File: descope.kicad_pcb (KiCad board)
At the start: 2 copper layers, 26.9 x 31.8 mm, 19 parts, among them Q1 2N3906, Q2 2N3904, Q3 2N3906, Q4 2N3904, Q5 2N3906, Q6 2N3904

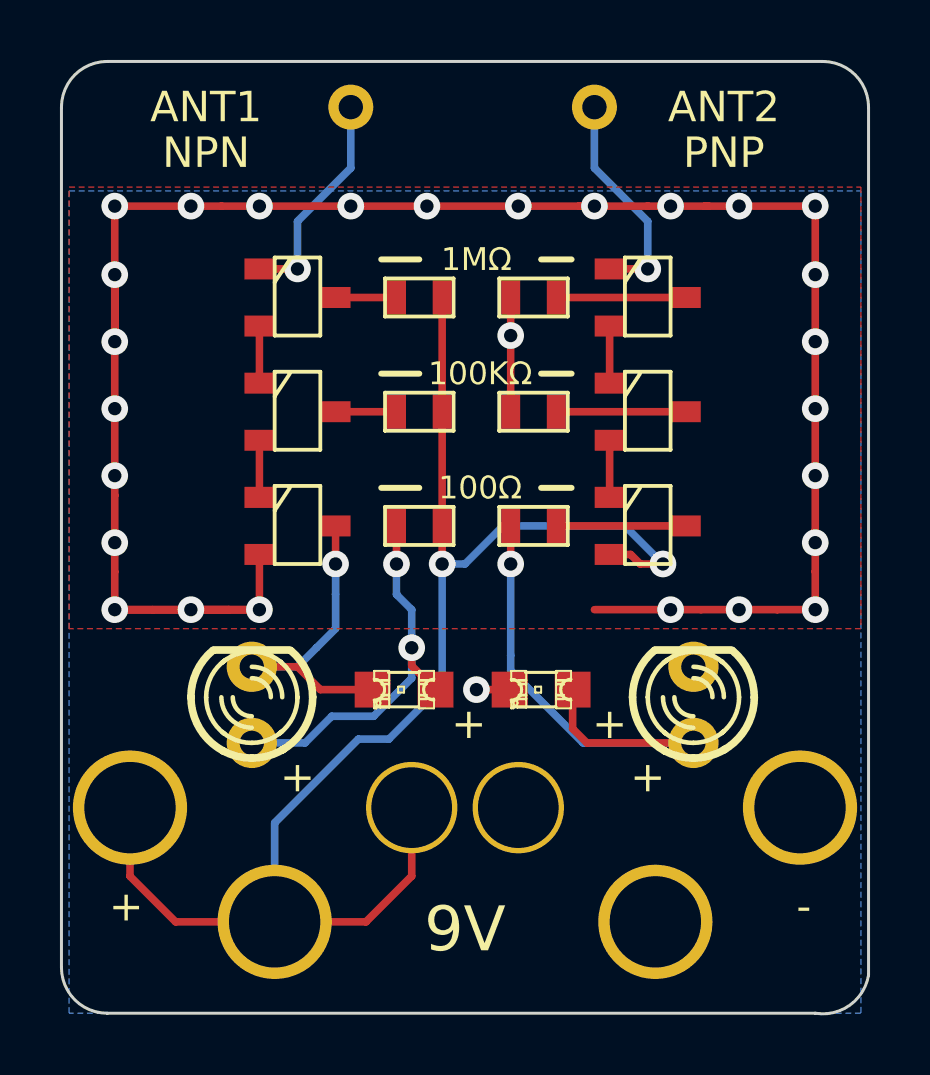
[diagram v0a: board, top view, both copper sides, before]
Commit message: Update electroscope for fabrication
Vendor: OSHPark, LLC
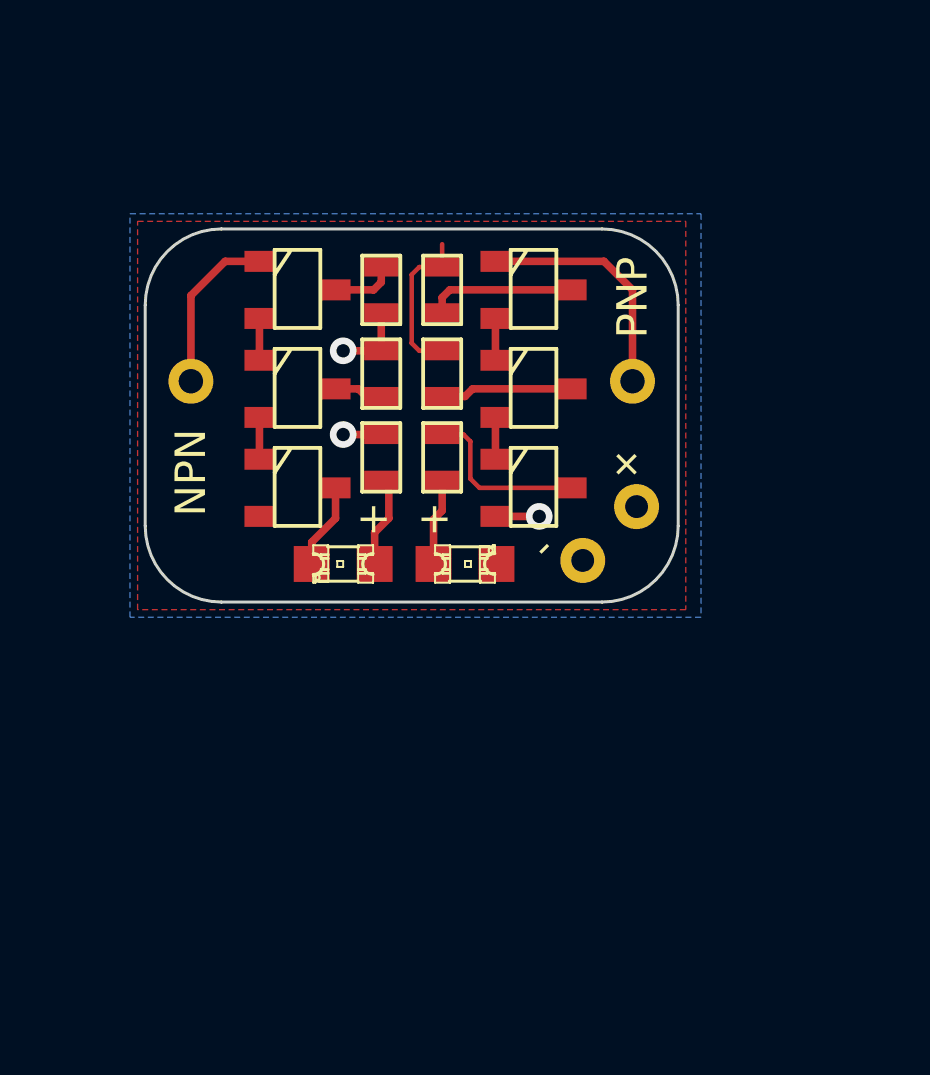
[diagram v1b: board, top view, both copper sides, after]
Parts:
- removed D3, D4: LED, LED-3MM
- BT1: footprint BSPCMF-9VBATT-SNAP -> BATT_CONN_SIMPLE
- moved ANT1 10.6 mm to (147.3, 177.3)
- moved BT1 10.1 mm to (161.3, 182.4), turned to 225 degrees
- moved ANT2 9.23 mm to (162.1, 177.3)
- moved D1 4.90 mm to (156.5, 183.4), turned to 0 degrees
- moved D2 4.66 mm to (152.4, 183.4)
- moved Q1 4.02 mm to (158.8, 180.8)
- moved Q3 3.89 mm to (158.8, 177.5)
- moved Q5 3.82 mm to (158.8, 174.2)
- moved R1 3.81 mm to (155.7, 179.8), turned to 270 degrees
- moved R3 3.30 mm to (155.7, 177.0), turned to 90 degrees
- moved R5 3.06 mm to (155.7, 174.2), turned to 90 degrees
- moved R6 2.62 mm to (153.7, 179.8), turned to 270 degrees
- moved R4 1.80 mm to (153.7, 177.0), turned to 270 degrees
- moved R2 1.30 mm to (153.7, 174.2), turned to 90 degrees
- moved Q6 1.27 mm to (150.9, 180.8)
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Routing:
- net GND: track 80.8 -> 5.29 mm, vias 28 -> 0
- net VCC: track 49.0 -> 5.52 mm, vias 2 -> 3
- net N-000007: track 17.2 -> 2.91 mm, vias 1 -> 0
- net N-0000011: track 13.0 -> 2.99 mm, vias 2 -> 0
- net N-000008: track 10.8 -> 2.87 mm, vias 1 -> 0
- net N-000001: track 7.40 -> 5.62 mm, vias 1 -> 0
- net N-0000015: track 4.32 -> 5.78 mm
- net N-0000013: track 4.32 -> 4.93 mm
- net N-0000012: track 7.40 -> 8.01 mm, vias 1 -> 0
- net N-000004: track 1.91 -> 1.40 mm
- net N-000002: track 1.91 -> 1.40 mm
- net N-000005: track 1.91 -> 1.40 mm
- net N-0000016: track 1.91 -> 1.40 mm
- added copper zone on B.Cu, net VCC
- removed copper zone on B.Cu, net GND
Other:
- board size 26.9 x 31.8 mm -> 17.8 x 12.4 mm
- net class Min added: clearance 0.1524, trace_width 0.1524, via_dia 0.508, via_drill 0.3302
- rule via_min_drill: 0.508 -> 0.3302
- rule via_min_size: 0.3302 -> 0.508
- board text added: "Smaller Toy Electroscope open.konspyre.org/selectro 2014-08-18 Power: 9V"
- board text removed: "2N3904"
- board text removed: "2N3906"
- board text removed: "Toy Electroscope Git: 10acfe2 2014-05-14"

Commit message: Eliminate copper pours
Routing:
- net GND: track 5.29 -> 26.6 mm, vias 0 -> 1
- net VCC: track 5.52 -> 20.4 mm
- removed copper zone on F.Cu, net GND
- removed copper zone on B.Cu, net VCC
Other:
- net class Default: clearance 0.254 -> 0.1524
- rule trace_clearance: 0.254 -> 0.1524
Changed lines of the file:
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@@
     (area 141.939223 168.5925 166.369888 185.4835)
     (thickness 1.6)
-    (drawings 13)
-    (tracks 49)
+    (drawings 17)
+    (tracks 71)
     (zones 0)
     (modules 17)
@@
   (layers
     (15 F.Cu signal)
-    (0 B.Cu signal)
+    (0 B.Cu signal hide)
     (16 B.Adhes user)
     (17 F.Adhes user)
@@
   (setup
     (last_trace_width 0.254)
-    (trace_clearance 0.254)
+    (user_trace_width 0.1524)
+    (user_trace_width 0.1778)
+    (user_trace_width 0.2032)
+    (user_trace_width 0.2286)
+    (user_trace_width 0.254)
+    (trace_clearance 0.1524)
     (zone_clearance 0.1524)
     (zone_45_only no)
@@
   (net 16 VCC)
   (net_class Default "This is the default net class."
-    (clearance 0.254)
+    (clearance 0.1524)
     (trace_width 0.254)
     (via_dia 0.889)
@@
     (uvia_drill 0.127)
     (add_net "")
+    (add_net GND)
     (add_net N-000001)
     (add_net N-0000011)
@@
     (add_net N-0000013)
     (add_net N-0000014)
+    (add_net N-0000015)
     (add_net N-0000016)
     (add_net N-000002)
@@
     (uvia_dia 0.508)
     (uvia_drill 0.127)
-    (add_net GND)
-    (add_net N-0000015)
   )
   (module SOT23_INV (layer F.Cu)
@@
     )
   )
+  (gr_line (start 154.305 175.641) (end 153.035 175.641) (angle 90) (layer F.SilkS) (width 0.2))
+  (gr_line (start 155.067 175.641) (end 156.337 175.641) (angle 90) (layer F.SilkS) (width 0.2))
+  (gr_line (start 155.067 178.435) (end 156.337 178.435) (angle 90) (layer F.SilkS) (width 0.2))
+  (gr_line (start 153.035 178.435) (end 154.305 178.435) (angle 90) (layer F.SilkS) (width 0.2))
   (gr_text + (at 155.448 181.864) (layer F.SilkS)
     (effects (font (size 1.016 1.016) (thickness 0.254)))
@@
     (effects (font (size 1.016 1.016) (thickness 0.254)))
   )
-  (segment (start 155.702 173.482) (end 154.94 173.482) (width 0.1524) (layer F.Cu) (net 1))
-  (segment (start 154.94 176.276) (end 155.702 176.276) (width 0.1524) (layer F.Cu) (net 1))
-  (segment (start 154.686 176.022) (end 154.94 176.276) (width 0.1524) (layer F.Cu) (net 1))
-  (segment (start 154.686 173.736) (end 154.686 176.022) (width 0.1524) (layer F.Cu) (net 1))
-  (segment (start 154.94 173.482) (end 154.686 173.736) (width 0.1524) (layer F.Cu) (net 1))
-  (segment (start 155.702 173.482) (end 155.702 172.72) (width 0.1524) (layer F.Cu) (net 1))
+  (segment (start 149.606 181.8005) (end 150.4315 181.8005) (width 0.254) (layer F.Cu) (net 1) (status 400000))
+  (segment (start 154.432 179.832) (end 154.686 179.578) (width 0.254) (layer F.Cu) (net 1))
+  (segment (start 151.384 179.832) (end 154.432 179.832) (width 0.254) (layer F.Cu) (net 1))
+  (segment (start 150.876 180.34) (end 151.384 179.832) (width 0.254) (layer F.Cu) (net 1))
+  (segment (start 150.876 181.356) (end 150.876 180.34) (width 0.254) (layer F.Cu) (net 1))
+  (segment (start 150.4315 181.8005) (end 150.876 181.356) (width 0.254) (layer F.Cu) (net 1))
+  (segment (start 160.391974 183.270026) (end 159.121974 183.270026) (width 0.254) (layer F.Cu) (net 1))
+  (segment (start 159.121974 183.270026) (end 159.004 183.388) (width 0.254) (layer F.Cu) (net 1))
+  (segment (start 159.004 183.388) (end 157.51302 183.388) (width 0.254) (layer F.Cu) (net 1))
+  (segment (start 154.686 181.864) (end 154.686 182.88) (width 0.254) (layer B.Cu) (net 1))
+  (segment (start 154.686 182.88) (end 155.076026 183.270026) (width 0.254) (layer B.Cu) (net 1))
+  (segment (start 155.076026 183.270026) (end 160.391974 183.270026) (width 0.254) (layer B.Cu) (net 1))
+  (segment (start 154.686 179.578) (end 154.686 181.864) (width 0.254) (layer F.Cu) (net 1))
+  (via (at 154.686 181.864) (size 0.889) (layers F.Cu B.Cu) (net 1))
+  (segment (start 155.702 176.276) (end 154.94 176.276) (width 0.254) (layer F.Cu) (net 1))
+  (segment (start 154.94 176.276) (end 154.686 176.53) (width 0.254) (layer F.Cu) (net 1))
+  (segment (start 154.686 176.53) (end 154.686 179.578) (width 0.254) (layer F.Cu) (net 1))
+  (segment (start 155.702 173.482) (end 154.94 173.482) (width 0.254) (layer F.Cu) (net 1))
+  (segment (start 154.94 173.482) (end 154.686 173.736) (width 0.254) (layer F.Cu) (net 1))
+  (segment (start 154.686 173.736) (end 154.686 176.022) (width 0.254) (layer F.Cu) (net 1))
+  (segment (start 154.686 176.022) (end 154.94 176.276) (width 0.254) (layer F.Cu) (net 1))
   (segment (start 148.463 173.2915) (end 149.606 173.2915) (width 0.254) (layer F.Cu) (net 2))
   (segment (start 147.32 174.4345) (end 148.463 173.2915) (width 0.254) (layer F.Cu) (net 2))
@@
   (segment (start 156.718 177.546) (end 160.02 177.546) (width 0.254) (layer F.Cu) (net 6))
   (segment (start 156.464 177.8) (end 156.718 177.546) (width 0.254) (layer F.Cu) (net 6))
-  (segment (start 155.702 179.07) (end 156.4132 179.07) (width 0.1524) (layer F.Cu) (net 7))
-  (segment (start 156.9466 180.848) (end 160.02 180.848) (width 0.1524) (layer F.Cu) (net 7))
-  (segment (start 156.6418 180.5432) (end 156.9466 180.848) (width 0.1524) (layer F.Cu) (net 7))
-  (segment (start 156.6418 179.2986) (end 156.6418 180.5432) (width 0.1524) (layer F.Cu) (net 7))
-  (segment (start 156.4132 179.07) (end 156.6418 179.2986) (width 0.1524) (layer F.Cu) (net 7))
+  (segment (start 155.702 179.07) (end 156.4132 179.07) (width 0.254) (layer F.Cu) (net 7))
+  (segment (start 156.4132 179.07) (end 156.6418 179.2986) (width 0.254) (layer F.Cu) (net 7))
+  (segment (start 156.6418 179.2986) (end 156.6418 180.5432) (width 0.254) (layer F.Cu) (net 7))
+  (segment (start 156.6418 180.5432) (end 156.9466 180.848) (width 0.254) (layer F.Cu) (net 7))
+  (segment (start 156.9466 180.848) (end 160.02 180.848) (width 0.254) (layer F.Cu) (net 7))
   (segment (start 157.48 175.1965) (end 157.48 176.5935) (width 0.254) (layer F.Cu) (net 8))
   (segment (start 157.48 178.4985) (end 157.48 179.8955) (width 0.254) (layer F.Cu) (net 9))
@@
   (segment (start 155.702 181.61) (end 155.702 180.594) (width 0.254) (layer F.Cu) (net 14))
   (segment (start 155.41498 181.89702) (end 155.702 181.61) (width 0.254) (layer F.Cu) (net 14))
-  (segment (start 151.35098 183.388) (end 151.35098 182.65902) (width 0.254) (layer F.Cu) (net 15))
-  (segment (start 152.146 181.864) (end 152.146 180.848) (width 0.254) (layer F.Cu) (net 15))
-  (segment (start 151.35098 182.65902) (end 152.146 181.864) (width 0.254) (layer F.Cu) (net 15))
-  (segment (start 153.67 176.276) (end 152.4 176.276) (width 0.254) (layer F.Cu) (net 16))
+  (segment (start 151.35098 183.388) (end 151.35098 182.40502) (width 0.254) (layer F.Cu) (net 15))
+  (segment (start 152.146 181.61) (end 152.146 180.848) (width 0.254) (layer F.Cu) (net 15))
+  (segment (start 151.35098 182.40502) (end 152.146 181.61) (width 0.254) (layer F.Cu) (net 15))
+  (segment (start 158.9405 180.0225) (end 158.9405 181.8005) (width 0.254) (layer B.Cu) (net 16))
+  (segment (start 157.988 179.07) (end 158.9405 180.0225) (width 0.254) (layer B.Cu) (net 16))
+  (segment (start 152.4 179.07) (end 157.988 179.07) (width 0.254) (layer B.Cu) (net 16))
+  (segment (start 162.188026 181.473974) (end 160.664026 181.473974) (width 0.254) (layer B.Cu) (net 16))
+  (segment (start 160.664026 181.473974) (end 160.3375 181.8005) (width 0.254) (layer B.Cu) (net 16))
+  (segment (start 160.3375 181.8005) (end 158.9405 181.8005) (width 0.254) (layer B.Cu) (net 16))
+  (via (at 158.9405 181.8005) (size 0.889) (layers F.Cu B.Cu) (net 16))
+  (segment (start 158.9405 181.8005) (end 157.48 181.8005) (width 0.254) (layer F.Cu) (net 16))
+  (segment (start 152.4 176.276) (end 152.4 179.07) (width 0.254) (layer B.Cu) (net 16))
+  (segment (start 152.4 176.276) (end 153.67 176.276) (width 0.254) (layer F.Cu) (net 16))
   (via (at 152.4 176.276) (size 0.889) (layers F.Cu B.Cu) (net 16))
+  (via (at 152.4 179.07) (size 0.889) (layers F.Cu B.Cu) (net 16))
+  (segment (start 153.924 179.07) (end 152.4 179.07) (width 0.254) (layer F.Cu) (net 16))
   (segment (start 153.67 175.006) (end 153.67 176.276) (width 0.254) (layer F.Cu) (net 16))
-  (segment (start 157.48 181.8005) (end 158.9405 181.8005) (width 0.254) (layer F.Cu) (net 16))
-  (via (at 158.9405 181.8005) (size 0.889) (layers F.Cu B.Cu) (net 16))
-  (segment (start 153.924 179.07) (end 152.4 179.07) (width 0.254) (layer F.Cu) (net 16))
-  (via (at 152.4 179.07) (size 0.889) (layers F.Cu B.Cu) (net 16))
-  (zone (net 16) (net_name VCC) (layer B.Cu) (hatch edge 0.508)
-    (connect_pads (clearance 0.2032))
-    (min_thickness 0.2032)
-    (fill (arc_segments 32) (thermal_gap 0.508) (thermal_bridge_width 0.508))
-    (polygon
-      (pts
-        (xy 164.338 185.166) (xy 145.288 185.166) (xy 145.288 171.704) (xy 164.338 171.704)
-      )
-    )
-  )
-  (zone (net 1) (net_name GND) (layer F.Cu) (hatch edge 0.508)
-    (connect_pads (clearance 0.1524))
-    (min_thickness 0.1524)
-    (fill (arc_segments 32) (thermal_gap 0.508) (thermal_bridge_width 0.508))
-    (polygon
-      (pts
-        (xy 163.83 184.912) (xy 145.542 184.912) (xy 145.542 171.958) (xy 163.83 171.958)
-      )
-    )
-  )
 )

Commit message: No copper pours version
Fabricator: OSHPark, LLC
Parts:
- added BT1: BATTERY, BATT_CONN_SIMPLE, B.Cu at (148.1, 182.4)
- added G***: OSHW-logo_silkscreen_5mm, OSHW-logo_silkscreen_5mm, B.Cu at (154.7, 181.6)
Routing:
- net VCC: track 20.4 -> 27.1 mm
- net GND: track 26.6 -> 28.4 mm
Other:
- board text added: "Smaller Toy Electroscope open.konspyre.org/selectro 2014-08-31 V+: 9V"
- board text removed: "Smaller Toy Electroscope open.konspyre.org/selectro 2014-08-18 Power: 9V"

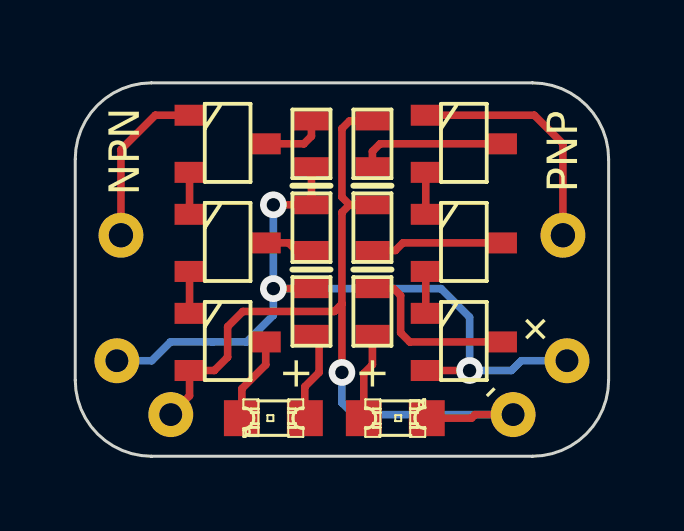
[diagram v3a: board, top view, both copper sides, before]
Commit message: Restore copper planes, keeping most recent features as well
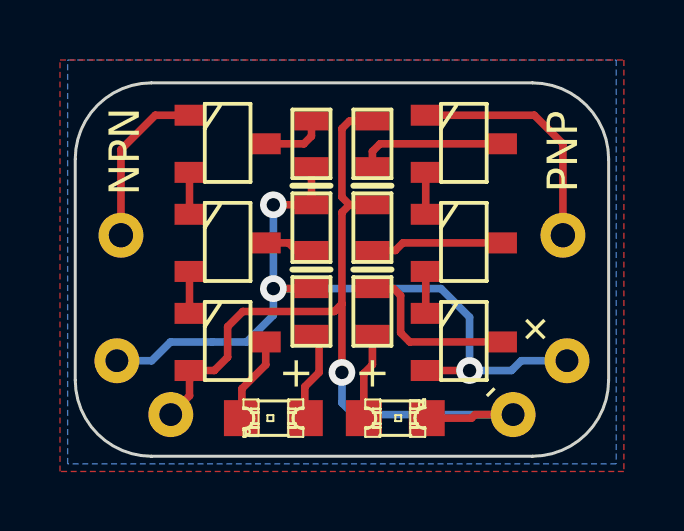
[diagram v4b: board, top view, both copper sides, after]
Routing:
- added copper zone on F.Cu, net GND
- added copper zone on B.Cu, net VCC
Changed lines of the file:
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@@
   (segment (start 153.924 179.07) (end 152.4 179.07) (width 0.254) (layer F.Cu) (net 16))
   (segment (start 153.67 175.006) (end 153.67 176.276) (width 0.254) (layer F.Cu) (net 16))
+  (zone (net 16) (net_name VCC) (layer B.Cu) (hatch edge 0.508)
+    (connect_pads (clearance 0.1524))
+    (min_thickness 0.1524)
+    (fill (arc_segments 16) (thermal_gap 0.508) (thermal_bridge_width 0.3))
+    (polygon
+      (pts
+        (xy 163.83 184.912) (xy 145.542 184.912) (xy 145.542 171.45) (xy 163.83 171.45)
+      )
+    )
+  )
+  (zone (net 1) (net_name GND) (layer F.Cu) (hatch edge 0.508)
+    (connect_pads (clearance 0.1524))
+    (min_thickness 0.1524)
+    (fill (arc_segments 16) (thermal_gap 0.508) (thermal_bridge_width 0.3))
+    (polygon
+      (pts
+        (xy 164.084 185.166) (xy 145.288 185.166) (xy 145.288 171.45) (xy 164.084 171.45)
+      )
+    )
+  )
 )
